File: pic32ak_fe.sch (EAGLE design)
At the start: 102 parts, among them IC1 NCP1117LPST33T3G, IC2 SFH6916, IC3 NCP51460SN33T1G, J1 CONBNC001, J2 CONBNC001, J3 CONBNC001, J4 CONBNC001, J5 5227222-3, SW1 PTS635SL50LFS, SW2 PTS635SL50LFS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

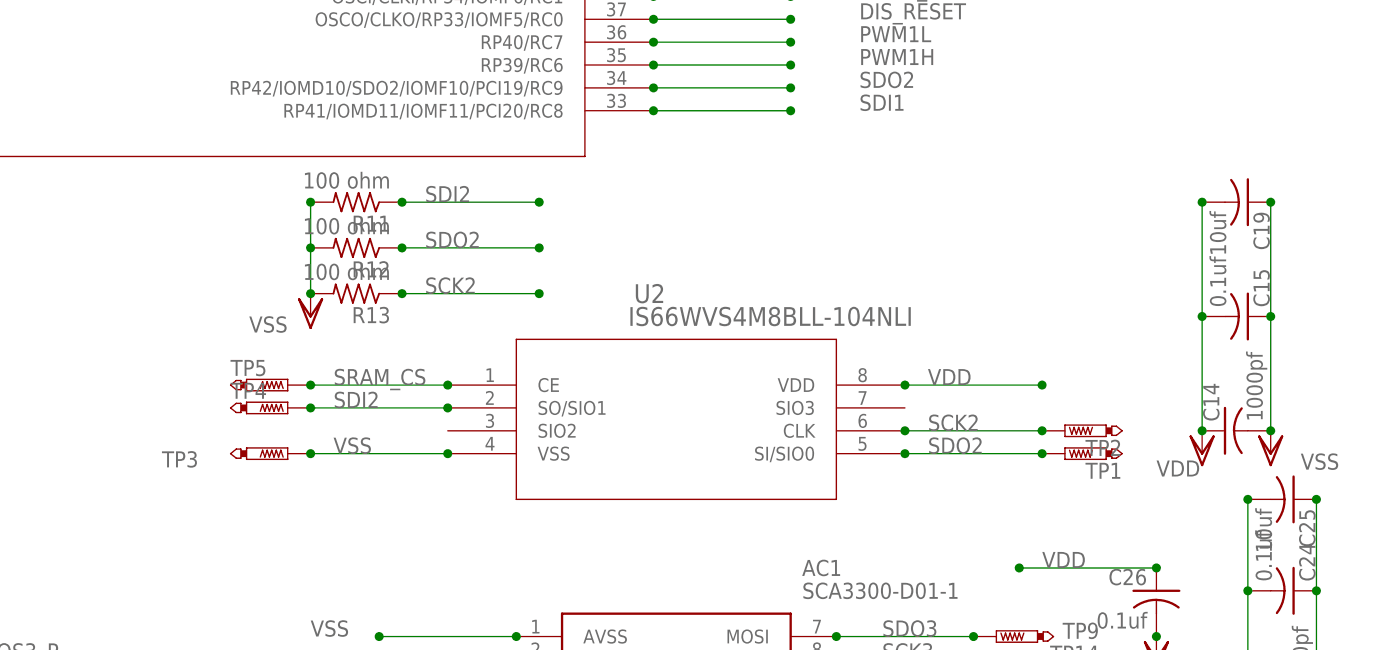
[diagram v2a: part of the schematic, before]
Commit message: max SPI2 speed
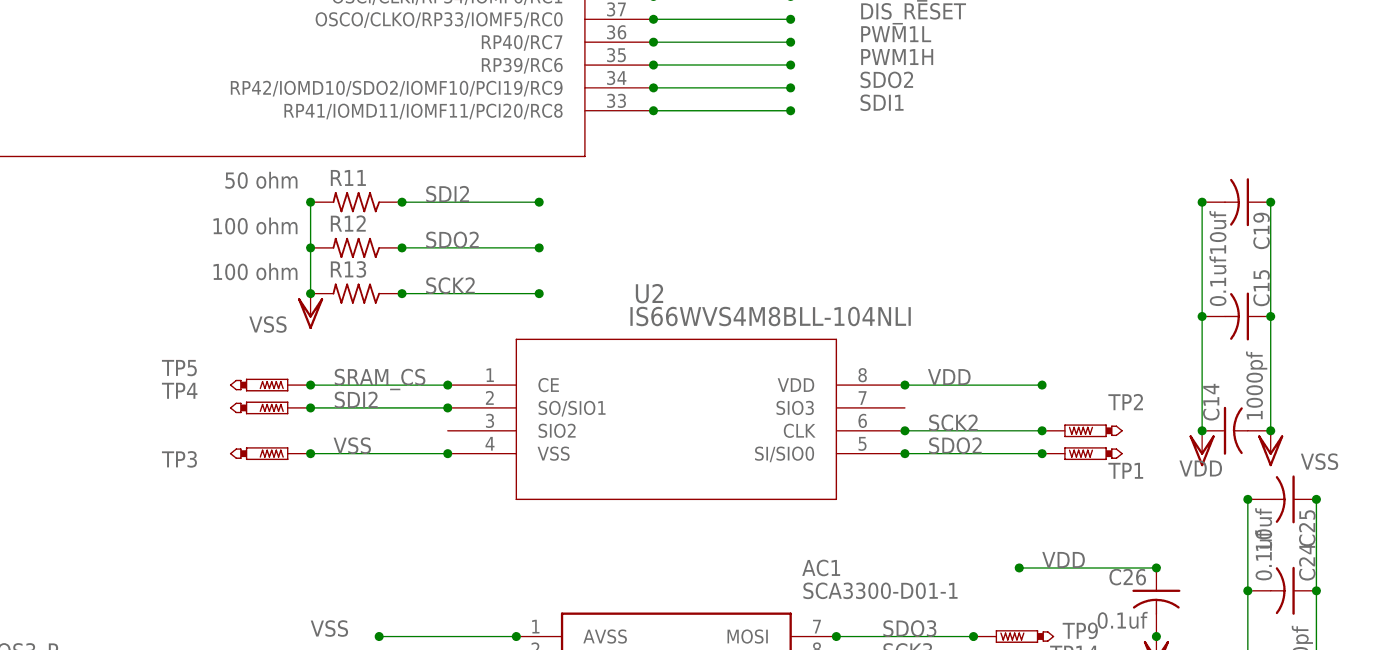
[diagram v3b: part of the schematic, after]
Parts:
- R11: value 100 ohm -> 50 ohm
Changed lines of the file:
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@@
 <part name="TP23" library="testpad" library_urn="urn:adsk.eagle:library:385" deviceset="PTR1" device="PAD1-13" package3d_urn="urn:adsk.eagle:package:27946/1"/>
 <part name="TP24" library="testpad" library_urn="urn:adsk.eagle:library:385" deviceset="PTR1" device="PAD1-13" package3d_urn="urn:adsk.eagle:package:27946/1"/>
-<part name="R11" library="rcl" library_urn="urn:adsk.eagle:library:334" deviceset="R-US_" device="R0805" package3d_urn="urn:adsk.eagle:package:23553/2" value="100 ohm"/>
+<part name="R11" library="rcl" library_urn="urn:adsk.eagle:library:334" deviceset="R-US_" device="R0805" package3d_urn="urn:adsk.eagle:package:23553/2" value="50 ohm"/>
 <part name="R12" library="rcl" library_urn="urn:adsk.eagle:library:334" deviceset="R-US_" device="R0805" package3d_urn="urn:adsk.eagle:package:23553/2" value="100 ohm"/>
 <part name="R13" library="rcl" library_urn="urn:adsk.eagle:library:334" deviceset="R-US_" device="R0805" package3d_urn="urn:adsk.eagle:package:23553/2" value="100 ohm"/>
@@
 </instance>
 <instance part="VDD4" gate="G$1" x="355.6" y="-71.12" smashed="yes" rot="R180">
-<attribute name="VALUE" x="350.52" y="-73.66" size="1.778" layer="96"/>
+<attribute name="VALUE" x="353.06" y="-73.66" size="1.778" layer="96"/>
 </instance>
 <instance part="VSS10" gate="G$1" x="363.22" y="-71.12" smashed="yes">
@@
 </instance>
 <instance part="TP1" gate="G$1" x="340.36" y="-71.12" smashed="yes" rot="R90">
-<attribute name="NAME" x="346.71" y="-72.136" size="1.778" layer="95" rot="R180"/>
+<attribute name="NAME" x="349.25" y="-72.136" size="1.778" layer="95" rot="R180"/>
 <attribute name="TP_SIGNAL_NAME" x="342.9" y="-69.85" size="1.778" layer="97" rot="R90"/>
 </instance>
 <instance part="TP2" gate="G$1" x="340.36" y="-68.58" smashed="yes" rot="R90">
-<attribute name="NAME" x="346.71" y="-69.596" size="1.778" layer="95" rot="R180"/>
+<attribute name="NAME" x="349.25" y="-64.516" size="1.778" layer="95" rot="R180"/>
 <attribute name="TP_SIGNAL_NAME" x="342.9" y="-67.31" size="1.778" layer="97" rot="R90"/>
 </instance>
@@
 </instance>
 <instance part="TP4" gate="G$1" x="254" y="-66.04" smashed="yes" rot="R270">
-<attribute name="NAME" x="247.65" y="-65.024" size="1.778" layer="95"/>
+<attribute name="NAME" x="240.03" y="-65.024" size="1.778" layer="95"/>
 <attribute name="TP_SIGNAL_NAME" x="251.46" y="-67.31" size="1.778" layer="97" rot="R270"/>
 </instance>
 <instance part="TP5" gate="G$1" x="254" y="-63.5" smashed="yes" rot="R270">
-<attribute name="NAME" x="247.65" y="-62.484" size="1.778" layer="95"/>
+<attribute name="NAME" x="240.03" y="-62.484" size="1.778" layer="95"/>
 <attribute name="TP_SIGNAL_NAME" x="251.46" y="-64.77" size="1.778" layer="97" rot="R270"/>
 </instance>
@@
 </instance>
 <instance part="R11" gate="G$1" x="261.62" y="-43.18" smashed="yes" rot="R180">
-<attribute name="NAME" x="265.43" y="-44.6786" size="1.778" layer="95" rot="R180"/>
-<attribute name="VALUE" x="265.43" y="-39.878" size="1.778" layer="96" rot="R180"/>
+<attribute name="NAME" x="262.89" y="-39.5986" size="1.778" layer="95" rot="R180"/>
+<attribute name="VALUE" x="255.27" y="-39.878" size="1.778" layer="96" rot="R180"/>
 </instance>
 <instance part="R12" gate="G$1" x="261.62" y="-48.26" smashed="yes" rot="R180">
-<attribute name="NAME" x="265.43" y="-49.7586" size="1.778" layer="95" rot="R180"/>
-<attribute name="VALUE" x="265.43" y="-44.958" size="1.778" layer="96" rot="R180"/>
+<attribute name="NAME" x="262.89" y="-44.6786" size="1.778" layer="95" rot="R180"/>
+<attribute name="VALUE" x="255.27" y="-44.958" size="1.778" layer="96" rot="R180"/>
 </instance>
 <instance part="R13" gate="G$1" x="261.62" y="-53.34" smashed="yes" rot="R180">
-<attribute name="NAME" x="265.43" y="-54.8386" size="1.778" layer="95" rot="R180"/>
-<attribute name="VALUE" x="265.43" y="-50.038" size="1.778" layer="96" rot="R180"/>
+<attribute name="NAME" x="262.89" y="-49.7586" size="1.778" layer="95" rot="R180"/>
+<attribute name="VALUE" x="255.27" y="-50.038" size="1.778" layer="96" rot="R180"/>
 </instance>
 <instance part="VSS39" gate="G$1" x="256.54" y="-55.88" smashed="yes">

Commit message: up
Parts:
- added USBC-PWR: USBC-PWR, con-lstb:MA04-1
- R12, R13: value 100 ohm -> 50 ohm
- renumbered TP3 to TP3_VSS
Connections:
- net RA8: now also GLCD.9
- net RA9: now also GLCD.10
- net VIN_PWR: now also USBC-PWR.4
- net VSS: now also USBC-PWR.1
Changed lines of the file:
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@@
 <part name="TP1" library="testpad" library_urn="urn:adsk.eagle:library:385" deviceset="PTR1" device="PAD1-13" package3d_urn="urn:adsk.eagle:package:27946/1"/>
 <part name="TP2" library="testpad" library_urn="urn:adsk.eagle:library:385" deviceset="PTR1" device="PAD1-13" package3d_urn="urn:adsk.eagle:package:27946/1"/>
-<part name="TP3" library="testpad" library_urn="urn:adsk.eagle:library:385" deviceset="PTR1" device="PAD1-13" package3d_urn="urn:adsk.eagle:package:27946/1"/>
+<part name="TP3_VSS" library="testpad" library_urn="urn:adsk.eagle:library:385" deviceset="PTR1" device="PAD1-13" package3d_urn="urn:adsk.eagle:package:27946/1"/>
 <part name="TP4" library="testpad" library_urn="urn:adsk.eagle:library:385" deviceset="PTR1" device="PAD1-13" package3d_urn="urn:adsk.eagle:package:27946/1"/>
 <part name="TP5" library="testpad" library_urn="urn:adsk.eagle:library:385" deviceset="PTR1" device="PAD1-13" package3d_urn="urn:adsk.eagle:package:27946/1"/>
@@
 <part name="TP24" library="testpad" library_urn="urn:adsk.eagle:library:385" deviceset="PTR1" device="PAD1-13" package3d_urn="urn:adsk.eagle:package:27946/1"/>
 <part name="R11" library="rcl" library_urn="urn:adsk.eagle:library:334" deviceset="R-US_" device="R0805" package3d_urn="urn:adsk.eagle:package:23553/2" value="50 ohm"/>
-<part name="R12" library="rcl" library_urn="urn:adsk.eagle:library:334" deviceset="R-US_" device="R0805" package3d_urn="urn:adsk.eagle:package:23553/2" value="100 ohm"/>
-<part name="R13" library="rcl" library_urn="urn:adsk.eagle:library:334" deviceset="R-US_" device="R0805" package3d_urn="urn:adsk.eagle:package:23553/2" value="100 ohm"/>
+<part name="R12" library="rcl" library_urn="urn:adsk.eagle:library:334" deviceset="R-US_" device="R0805" package3d_urn="urn:adsk.eagle:package:23553/2" value="50 ohm"/>
+<part name="R13" library="rcl" library_urn="urn:adsk.eagle:library:334" deviceset="R-US_" device="R0805" package3d_urn="urn:adsk.eagle:package:23553/2" value="50 ohm"/>
 <part name="VSS39" library="supply1" library_urn="urn:adsk.eagle:library:371" deviceset="VSS" device=""/>
 <part name="IC3" library="NCP51460SN33T1G" deviceset="NCP51460SN33T1G" device=""/>
@@
 <part name="C28" library="rcl" library_urn="urn:adsk.eagle:library:334" deviceset="C-US" device="C0603" package3d_urn="urn:adsk.eagle:package:23616/2" value="0.1uf"/>
 <part name="VSS42" library="supply1" library_urn="urn:adsk.eagle:library:371" deviceset="VSS" device=""/>
+<part name="USBC-PWR" library="con-lstb" library_urn="urn:adsk.eagle:library:162" deviceset="MA04-1" device="" package3d_urn="urn:adsk.eagle:package:8337/1" value="USBC-PWR"/>
+<part name="VSS43" library="supply1" library_urn="urn:adsk.eagle:library:371" deviceset="VSS" device=""/>
 </parts>
 <sheets>
@@
 <attribute name="NAME" x="123.19" y="-47.498" size="1.778" layer="95"/>
 </instance>
-<instance part="VSS1" gate="G$1" x="147.32" y="-53.34" smashed="yes" rot="R180">
-<attribute name="VALUE" x="149.86" y="-53.34" size="1.778" layer="96"/>
+<instance part="VSS1" gate="G$1" x="149.86" y="-53.34" smashed="yes" rot="R180">
+<attribute name="VALUE" x="152.4" y="-53.34" size="1.778" layer="96"/>
 </instance>
 <instance part="VDD1" gate="G$1" x="152.4" y="-55.88" smashed="yes">
@@
 <attribute name="TP_SIGNAL_NAME" x="342.9" y="-67.31" size="1.778" layer="97" rot="R90"/>
 </instance>
-<instance part="TP3" gate="G$1" x="254" y="-71.12" smashed="yes" rot="R270">
-<attribute name="NAME" x="240.03" y="-72.644" size="1.778" layer="95"/>
+<instance part="TP3_VSS" gate="G$1" x="254" y="-71.12" smashed="yes" rot="R270">
+<attribute name="NAME" x="234.95" y="-72.644" size="1.778" layer="95"/>
 <attribute name="TP_SIGNAL_NAME" x="251.46" y="-72.39" size="1.778" layer="97" rot="R270"/>
 </instance>
@@
 <instance part="VSS42" gate="G$1" x="63.5" y="99.06" smashed="yes">
 <attribute name="VALUE" x="60.96" y="99.06" size="1.778" layer="96" rot="R180"/>
+</instance>
+<instance part="USBC-PWR" gate="1" x="35.56" y="-99.06" smashed="yes">
+<attribute name="VALUE" x="34.29" y="-109.22" size="1.778" layer="96"/>
+<attribute name="NAME" x="34.29" y="-93.218" size="1.778" layer="95"/>
+</instance>
+<instance part="VSS43" gate="G$1" x="43.18" y="-106.68" smashed="yes">
+<attribute name="VALUE" x="40.64" y="-106.68" size="1.778" layer="96" rot="R180"/>
 </instance>
 </instances>
@@
 <segment>
 <pinref part="GLCD" gate="1" pin="8"/>
-<wire x1="132.08" y1="-55.88" x2="147.32" y2="-55.88" width="0.1524" layer="91"/>
+<wire x1="132.08" y1="-55.88" x2="149.86" y2="-55.88" width="0.1524" layer="91"/>
 <pinref part="VSS1" gate="G$1" pin="VSS"/>
 <junction x="132.08" y="-55.88"/>
-<junction x="147.32" y="-55.88"/>
+<junction x="149.86" y="-55.88"/>
 </segment>
 <segment>
@@
 <pinref part="U2" gate="A" pin="VSS"/>
 <junction x="271.78" y="-71.12"/>
-<pinref part="TP3" gate="G$1" pin="TP"/>
+<pinref part="TP3_VSS" gate="G$1" pin="TP"/>
 </segment>
 <segment>
@@
 <pinref part="LED2" gate="G$1" pin="C"/>
 <pinref part="VSS17" gate="G$1" pin="VSS"/>
+<junction x="241.3" y="76.2"/>
 </segment>
 <segment>
 <pinref part="LED3" gate="G$1" pin="C"/>
 <pinref part="VSS18" gate="G$1" pin="VSS"/>
+<junction x="248.92" y="76.2"/>
 </segment>
 <segment>
 <pinref part="LED4" gate="G$1" pin="C"/>
 <pinref part="VSS19" gate="G$1" pin="VSS"/>
+<junction x="256.54" y="76.2"/>
 </segment>
 <segment>
@@
 <pinref part="R10" gate="G$1" pin="1"/>
 <pinref part="VSS25" gate="G$1" pin="VSS"/>
+<junction x="5.08" y="-38.1"/>
 </segment>
 <segment>
@@
 <junction x="63.5" y="101.6"/>
 </segment>
+<segment>
+<pinref part="USBC-PWR" gate="1" pin="1"/>
+<pinref part="VSS43" gate="G$1" pin="VSS"/>
+<junction x="43.18" y="-104.14"/>
+</segment>
 </net>
 <net name="SDI1" class="0">
@@
 <pinref part="R3" gate="G$1" pin="1"/>
 <pinref part="POWER" gate="G$1" pin="A"/>
+<junction x="233.68" y="83.82"/>
 </segment>
 </net>
@@
 <pinref part="LED2" gate="G$1" pin="A"/>
 <pinref part="R4" gate="G$1" pin="1"/>
+<junction x="241.3" y="83.82"/>
 </segment>
 </net>
@@
 <pinref part="LED3" gate="G$1" pin="A"/>
 <pinref part="R5" gate="G$1" pin="1"/>
+<junction x="248.92" y="83.82"/>
 </segment>
 </net>
@@
 <pinref part="LED4" gate="G$1" pin="A"/>
 <pinref part="R6" gate="G$1" pin="1"/>
+<junction x="256.54" y="83.82"/>
 </segment>
 </net>
@@
 <junction x="73.66" y="-91.44"/>
 </segment>
+<segment>
+<wire x1="43.18" y1="-96.52" x2="50.8" y2="-96.52" width="0.1524" layer="91"/>
+<pinref part="USBC-PWR" gate="1" pin="4"/>
+<junction x="43.18" y="-96.52"/>
+<junction x="50.8" y="-96.52"/>
+<label x="45.72" y="-96.52" size="1.778" layer="95"/>
+</segment>
 </net>
 <net name="OA2IN" class="0">
@@
 <label x="91.44" y="-106.68" size="1.778" layer="95"/>
 </segment>
+<segment>
+<wire x1="147.32" y1="-53.34" x2="132.08" y2="-53.34" width="0.1524" layer="91"/>
+<pinref part="GLCD" gate="1" pin="9"/>
+<junction x="132.08" y="-53.34"/>
+<junction x="147.32" y="-53.34"/>
+<label x="134.62" y="-53.34" size="1.778" layer="95"/>
+</segment>
 </net>
 <net name="RA9" class="0">
@@
 <label x="91.44" y="-104.14" size="1.778" layer="95"/>
 </segment>
-</net>
+<segment>
+<wire x1="147.32" y1="-50.8" x2="132.08" y2="-50.8" width="0.1524" layer="91"/>
+<pinref part="GLCD" gate="1" pin="10"/>
+<junction x="132.08" y="-50.8"/>
+<junction x="147.32" y="-50.8"/>
+<label x="134.62" y="-50.8" size="1.778" layer="95"/>
+</segment>
+</net>

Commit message: up
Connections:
- net RA11 renamed TEST_P1
- removed net RA8: GLCD.9, PWM.8, U1.AD2AN9/ISRC3/IBIAS3/RP9/RA8
- removed net RA9: GLCD.10, PWM.9, U1.AD1ANN3/AD1AN9/RP10/RA9
- removed net RB1: MISC_ANA.3, U1.TMS/OA2IN-/AD1AN4/AD2ANN1/RP18/RB1
- removed net RB5: MISC_ANA.4, U1.OA3IN+/AD2AN2/CMP3B/RP22/RB5
- new net RB1_DU: MISC_ANA.4, U1.TMS/OA2IN-/AD1AN4/AD2ANN1/RP18/RB1
- new net RC7: PWM.2, U1.RP40/RC7
- new net RC8: PWM.3, U1.RP39/RC6
- new net RD2: MISC_ANA.3, U1.TDO/RP51/PWM1H/IOMD4/RD2
- net DLED: now also U1.OA3IN+/AD2AN2/CMP3B/RP22/RB5; no longer U1.TDO/RP51/PWM1H/IOMD4/RD2
- net PWM1H: now also GLCD.10, PWM.9, U1.AD1ANN3/AD1AN9/RP10/RA9; no longer PWM.3, U1.RP39/RC6
- net PWM1L: now also GLCD.9, PWM.8, U1.AD2AN9/ISRC3/IBIAS3/RP9/RA8; no longer PWM.2, U1.RP40/RC7
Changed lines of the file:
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@@
 </segment>
 </net>
-<net name="DLED" class="0">
+<net name="RD2" class="0">
 <segment>
 <pinref part="U1" gate="A" pin="TDO/RP51/PWM1H/IOMD4/RD2"/>
@@
 <junction x="294.64" y="17.78"/>
 <junction x="309.88" y="17.78"/>
-<label x="317.5" y="17.78" size="1.778" layer="95"/>
-</segment>
-<segment>
-<wire x1="248.92" y1="93.98" x2="248.92" y2="109.22" width="0.1524" layer="91"/>
-<pinref part="R5" gate="G$1" pin="2"/>
-<junction x="248.92" y="93.98"/>
-<label x="248.92" y="101.6" size="1.778" layer="95" rot="R90"/>
-<junction x="248.92" y="109.22"/>
+<label x="302.26" y="17.78" size="1.778" layer="95"/>
+</segment>
+<segment>
+<wire x1="22.86" y1="55.88" x2="35.56" y2="55.88" width="0.1524" layer="91"/>
+<pinref part="MISC_ANA" gate="A" pin="3"/>
+<junction x="22.86" y="55.88"/>
+<junction x="35.56" y="55.88"/>
+<label x="38.1" y="55.88" size="1.778" layer="95"/>
 </segment>
 </net>
@@
 </segment>
 </net>
-<net name="RB1" class="0">
+<net name="RB1_DU" class="0">
 <segment>
 <pinref part="U1" gate="A" pin="TMS/OA2IN-/AD1AN4/AD2ANN1/RP18/RB1"/>
@@
 </segment>
 <segment>
-<wire x1="35.56" y1="55.88" x2="22.86" y2="55.88" width="0.1524" layer="91"/>
-<pinref part="MISC_ANA" gate="A" pin="3"/>
-<junction x="35.56" y="55.88"/>
-<label x="38.1" y="55.88" size="1.778" layer="95"/>
+<wire x1="35.56" y1="58.42" x2="22.86" y2="58.42" width="0.1524" layer="91"/>
+<pinref part="MISC_ANA" gate="A" pin="4"/>
+<junction x="22.86" y="58.42"/>
+<junction x="35.56" y="58.42"/>
+<label x="38.1" y="58.42" size="1.778" layer="95"/>
 </segment>
 </net>
@@
 </segment>
 </net>
-<net name="PWM1H" class="0">
+<net name="RC8" class="0">
 <segment>
 <pinref part="U1" gate="A" pin="RP39/RC6"/>
@@
 <junction x="294.64" y="-27.94"/>
 <junction x="309.88" y="-27.94"/>
-<label x="317.5" y="-27.94" size="1.778" layer="95"/>
+<label x="302.26" y="-27.94" size="1.778" layer="95"/>
 </segment>
 <segment>
@@
 </segment>
 </net>
-<net name="PWM1L" class="0">
+<net name="RC7" class="0">
 <segment>
 <pinref part="U1" gate="A" pin="RP40/RC7"/>
@@
 <junction x="294.64" y="-25.4"/>
 <junction x="309.88" y="-25.4"/>
-<label x="317.5" y="-25.4" size="1.778" layer="95"/>
+<label x="302.26" y="-25.4" size="1.778" layer="95"/>
 </segment>
 <segment>
@@
 </segment>
 </net>
-<net name="RA11" class="0">
+<net name="TEST_P1" class="0">
 <segment>
 <pinref part="U1" gate="A" pin="AD1AN10/RP12/RA11"/>
@@
 </segment>
 </net>
-<net name="RA8" class="0">
+<net name="PWM1L" class="0">
 <segment>
 <pinref part="U1" gate="A" pin="AD2AN9/ISRC3/IBIAS3/RP9/RA8"/>
@@
 <junction x="76.2" y="30.48"/>
 <junction x="60.96" y="30.48"/>
-<label x="66.04" y="30.48" size="1.778" layer="95"/>
+<label x="50.8" y="30.48" size="1.778" layer="95"/>
 </segment>
 <segment>
@@
 </segment>
 </net>
-<net name="RA9" class="0">
+<net name="PWM1H" class="0">
 <segment>
 <pinref part="U1" gate="A" pin="AD1ANN3/AD1AN9/RP10/RA9"/>
@@
 <junction x="76.2" y="27.94"/>
 <junction x="60.96" y="27.94"/>
-<label x="66.04" y="27.94" size="1.778" layer="95"/>
+<label x="50.8" y="27.94" size="1.778" layer="95"/>
 </segment>
 <segment>
@@
 </segment>
 </net>
-<net name="RB5" class="0">
+<net name="DLED" class="0">
 <segment>
 <pinref part="U1" gate="A" pin="OA3IN+/AD2AN2/CMP3B/RP22/RB5"/>
@@
 <junction x="60.96" y="5.08"/>
 <junction x="76.2" y="5.08"/>
-<label x="66.04" y="5.08" size="1.778" layer="95"/>
-</segment>
-<segment>
-<wire x1="35.56" y1="58.42" x2="22.86" y2="58.42" width="0.1524" layer="91"/>
-<pinref part="MISC_ANA" gate="A" pin="4"/>
-<junction x="22.86" y="58.42"/>
-<junction x="35.56" y="58.42"/>
-<label x="38.1" y="58.42" size="1.778" layer="95"/>
-</segment>
-</net>
+<label x="50.8" y="5.08" size="1.778" layer="95"/>
+</segment>
+<segment>
+<wire x1="248.92" y1="109.22" x2="248.92" y2="93.98" width="0.1524" layer="91"/>
+<pinref part="R5" gate="G$1" pin="2"/>
+<junction x="248.92" y="93.98"/>
+<junction x="248.92" y="109.22"/>
+<label x="248.92" y="101.6" size="1.778" layer="95" rot="R90"/>
+</segment>
+</net>
